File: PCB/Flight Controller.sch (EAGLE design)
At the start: 24 parts, among them J1 ZX62-AB-5PA(31), J2 M50-3600542R, U1 BMP390L, U2 NINA-B306, U3 LMS8117ADT-3.3, U4 BNO055

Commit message: added power and PWM pinheaders to schematic
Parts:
- added JP1: (no value), pinhead:PINHD-1X2
- added JP2, JP3: (no value), pinhead:PINHD-1X4
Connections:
- net GND: now also JP1.2, JP2.1, JP2.3, JP3.1, JP3.3
- net PWM0: now also JP2.2
- net PWM1: now also JP2.4
- net PWM2: now also JP3.2
- net PWM3: now also JP3.4
- net VCC: now also JP1.1
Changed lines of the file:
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@@
 <part name="GND16" library="supply1" library_urn="urn:adsk.eagle:library:371" deviceset="GND" device=""/>
 <part name="GND17" library="supply1" library_urn="urn:adsk.eagle:library:371" deviceset="GND" device=""/>
+<part name="JP1" library="pinhead" library_urn="urn:adsk.eagle:library:325" deviceset="PINHD-1X2" device="" package3d_urn="urn:adsk.eagle:package:22435/2"/>
+<part name="P+2" library="supply1" library_urn="urn:adsk.eagle:library:371" deviceset="VCC" device=""/>
+<part name="GND18" library="supply1" library_urn="urn:adsk.eagle:library:371" deviceset="GND" device=""/>
+<part name="JP2" library="pinhead" library_urn="urn:adsk.eagle:library:325" deviceset="PINHD-1X4" device="" package3d_urn="urn:adsk.eagle:package:22407/2"/>
+<part name="JP3" library="pinhead" library_urn="urn:adsk.eagle:library:325" deviceset="PINHD-1X4" device="" package3d_urn="urn:adsk.eagle:package:22407/2"/>
+<part name="GND19" library="supply1" library_urn="urn:adsk.eagle:library:371" deviceset="GND" device=""/>
+<part name="GND20" library="supply1" library_urn="urn:adsk.eagle:library:371" deviceset="GND" device=""/>
+<part name="GND21" library="supply1" library_urn="urn:adsk.eagle:library:371" deviceset="GND" device=""/>
+<part name="GND22" library="supply1" library_urn="urn:adsk.eagle:library:371" deviceset="GND" device=""/>
 </parts>
 <sheets>
@@
 <attribute name="VALUE" x="152.4" y="134.62" size="1.778" layer="96"/>
 </instance>
+<instance part="JP1" gate="G$1" x="45.72" y="137.16" smashed="yes" rot="R270">
+<attribute name="NAME" x="51.435" y="143.51" size="1.778" layer="95" rot="R270"/>
+<attribute name="VALUE" x="40.64" y="143.51" size="1.778" layer="96" rot="R270"/>
+</instance>
+<instance part="P+2" gate="VCC" x="50.8" y="152.4" smashed="yes">
+<attribute name="VALUE" x="48.26" y="149.86" size="1.778" layer="96" rot="R90"/>
+</instance>
+<instance part="GND18" gate="1" x="40.64" y="152.4" smashed="yes" rot="R180">
+<attribute name="VALUE" x="43.18" y="154.94" size="1.778" layer="96" rot="R180"/>
+</instance>
+<instance part="JP2" gate="A" x="342.9" y="139.7" smashed="yes">
+<attribute name="NAME" x="336.55" y="147.955" size="1.778" layer="95"/>
+<attribute name="VALUE" x="336.55" y="132.08" size="1.778" layer="96"/>
+</instance>
+<instance part="JP3" gate="A" x="342.9" y="121.92" smashed="yes">
+<attribute name="NAME" x="336.55" y="130.175" size="1.778" layer="95"/>
+<attribute name="VALUE" x="336.55" y="114.3" size="1.778" layer="96"/>
+</instance>
+<instance part="GND19" gate="1" x="314.96" y="139.7" smashed="yes">
+<attribute name="VALUE" x="312.42" y="137.16" size="1.778" layer="96"/>
+</instance>
+<instance part="GND20" gate="1" x="314.96" y="132.08" smashed="yes">
+<attribute name="VALUE" x="312.42" y="129.54" size="1.778" layer="96"/>
+</instance>
+<instance part="GND21" gate="1" x="314.96" y="121.92" smashed="yes">
+<attribute name="VALUE" x="312.42" y="119.38" size="1.778" layer="96"/>
+</instance>
+<instance part="GND22" gate="1" x="314.96" y="114.3" smashed="yes">
+<attribute name="VALUE" x="312.42" y="111.76" size="1.778" layer="96"/>
+</instance>
 </instances>
 <busses>
@@
 <wire x1="-10.16" y1="114.3" x2="-10.16" y2="109.22" width="0.1524" layer="91"/>
 <junction x="-10.16" y="114.3"/>
+</segment>
+<segment>
+<pinref part="JP1" gate="G$1" pin="1"/>
+<wire x1="48.26" y1="139.7" x2="48.26" y2="144.78" width="0.1524" layer="91"/>
+<wire x1="48.26" y1="144.78" x2="50.8" y2="144.78" width="0.1524" layer="91"/>
+<pinref part="P+2" gate="VCC" pin="VCC"/>
+<wire x1="50.8" y1="144.78" x2="50.8" y2="149.86" width="0.1524" layer="91"/>
 </segment>
 </net>
@@
 <pinref part="GND17" gate="1" pin="GND"/>
 </segment>
+<segment>
+<pinref part="GND18" gate="1" pin="GND"/>
+<wire x1="40.64" y1="149.86" x2="40.64" y2="144.78" width="0.1524" layer="91"/>
+<wire x1="40.64" y1="144.78" x2="45.72" y2="144.78" width="0.1524" layer="91"/>
+<pinref part="JP1" gate="G$1" pin="2"/>
+<wire x1="45.72" y1="144.78" x2="45.72" y2="139.7" width="0.1524" layer="91"/>
+</segment>
+<segment>
+<pinref part="JP2" gate="A" pin="1"/>
+<wire x1="340.36" y1="144.78" x2="314.96" y2="144.78" width="0.1524" layer="91"/>
+<pinref part="GND19" gate="1" pin="GND"/>
+<wire x1="314.96" y1="144.78" x2="314.96" y2="142.24" width="0.1524" layer="91"/>
+</segment>
+<segment>
+<pinref part="JP2" gate="A" pin="3"/>
+<wire x1="340.36" y1="139.7" x2="320.04" y2="139.7" width="0.1524" layer="91"/>
+<wire x1="320.04" y1="139.7" x2="320.04" y2="137.16" width="0.1524" layer="91"/>
+<wire x1="320.04" y1="137.16" x2="314.96" y2="137.16" width="0.1524" layer="91"/>
+<pinref part="GND20" gate="1" pin="GND"/>
+<wire x1="314.96" y1="137.16" x2="314.96" y2="134.62" width="0.1524" layer="91"/>
+</segment>
+<segment>
+<pinref part="GND21" gate="1" pin="GND"/>
+<wire x1="314.96" y1="124.46" x2="314.96" y2="127" width="0.1524" layer="91"/>
+<pinref part="JP3" gate="A" pin="1"/>
+<wire x1="314.96" y1="127" x2="340.36" y2="127" width="0.1524" layer="91"/>
+</segment>
+<segment>
+<pinref part="JP3" gate="A" pin="3"/>
+<wire x1="340.36" y1="121.92" x2="320.04" y2="121.92" width="0.1524" layer="91"/>
+<wire x1="320.04" y1="121.92" x2="320.04" y2="116.84" width="0.1524" layer="91"/>
+<pinref part="GND22" gate="1" pin="GND"/>
+<wire x1="320.04" y1="116.84" x2="314.96" y2="116.84" width="0.1524" layer="91"/>
+</segment>
 </net>
 <net name="D-" class="0">
@@
 <label x="246.38" y="55.88" size="1.778" layer="95"/>
 </segment>
+<segment>
+<pinref part="JP2" gate="A" pin="2"/>
+<wire x1="340.36" y1="142.24" x2="335.28" y2="142.24" width="0.1524" layer="91"/>
+<label x="327.66" y="142.24" size="1.778" layer="95"/>
+</segment>
 </net>
 <net name="PWM1" class="0">
@@
 <label x="246.38" y="53.34" size="1.778" layer="95"/>
 </segment>
+<segment>
+<pinref part="JP2" gate="A" pin="4"/>
+<wire x1="340.36" y1="137.16" x2="335.28" y2="137.16" width="0.1524" layer="91"/>
+<label x="327.66" y="137.16" size="1.778" layer="95"/>
+</segment>
 </net>
 <net name="PWM2" class="0">
@@
 <label x="246.38" y="50.8" size="1.778" layer="95"/>
 </segment>
+<segment>
+<pinref part="JP3" gate="A" pin="2"/>
+<wire x1="340.36" y1="124.46" x2="335.28" y2="124.46" width="0.1524" layer="91"/>
+<label x="327.66" y="124.46" size="1.778" layer="95"/>
+</segment>
 </net>
 <net name="PWM3" class="0">
@@
 <label x="246.38" y="48.26" size="1.778" layer="95"/>
 </segment>
-</net>
+<segment>
+<pinref part="JP3" gate="A" pin="4"/>
+<wire x1="340.36" y1="119.38" x2="335.28" y2="119.38" width="0.1524" layer="91"/>
+<label x="327.66" y="119.38" size="1.778" layer="95"/>
+</segment>
+</net>

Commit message: began routing PCB
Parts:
- added R8: 10k, rcl:R-US_R1206
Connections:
- net NRESET: now also R8.1
- net VDD: now also R8.2
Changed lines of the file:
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@@
 <part name="GND21" library="supply1" library_urn="urn:adsk.eagle:library:371" deviceset="GND" device=""/>
 <part name="GND22" library="supply1" library_urn="urn:adsk.eagle:library:371" deviceset="GND" device=""/>
+<part name="R8" library="rcl" library_urn="urn:adsk.eagle:library:334" deviceset="R-US_" device="R1206" package3d_urn="urn:adsk.eagle:package:23540/2" value="10k"/>
+<part name="VDD14" library="supply1" library_urn="urn:adsk.eagle:library:371" deviceset="VDD" device=""/>
 </parts>
 <sheets>
@@
 <instance part="GND22" gate="1" x="314.96" y="114.3" smashed="yes">
 <attribute name="VALUE" x="312.42" y="111.76" size="1.778" layer="96"/>
+</instance>
+<instance part="R8" gate="G$1" x="274.32" y="114.3" smashed="yes" rot="R90">
+<attribute name="NAME" x="272.8214" y="115.57" size="1.778" layer="95" rot="R90"/>
+<attribute name="VALUE" x="280.162" y="115.57" size="1.778" layer="96" rot="R90"/>
+</instance>
+<instance part="VDD14" gate="G$1" x="274.32" y="127" smashed="yes">
+<attribute name="VALUE" x="271.78" y="124.46" size="1.778" layer="96" rot="R90"/>
 </instance>
 </instances>
@@
 <wire x1="139.7" y1="162.56" x2="139.7" y2="154.94" width="0.1524" layer="91"/>
 <junction x="139.7" y="154.94"/>
+</segment>
+<segment>
+<pinref part="VDD14" gate="G$1" pin="VDD"/>
+<pinref part="R8" gate="G$1" pin="2"/>
+<wire x1="274.32" y1="124.46" x2="274.32" y2="119.38" width="0.1524" layer="91"/>
 </segment>
 </net>
@@
 <label x="246.38" y="86.36" size="1.778" layer="95"/>
 </segment>
-</net>
+<segment>
+<pinref part="R8" gate="G$1" pin="1"/>
+<wire x1="274.32" y1="109.22" x2="274.32" y2="104.14" width="0.1524" layer="91"/>
+<label x="276.86" y="104.14" size="1.778" layer="95"/>
+</segment>
+</net>

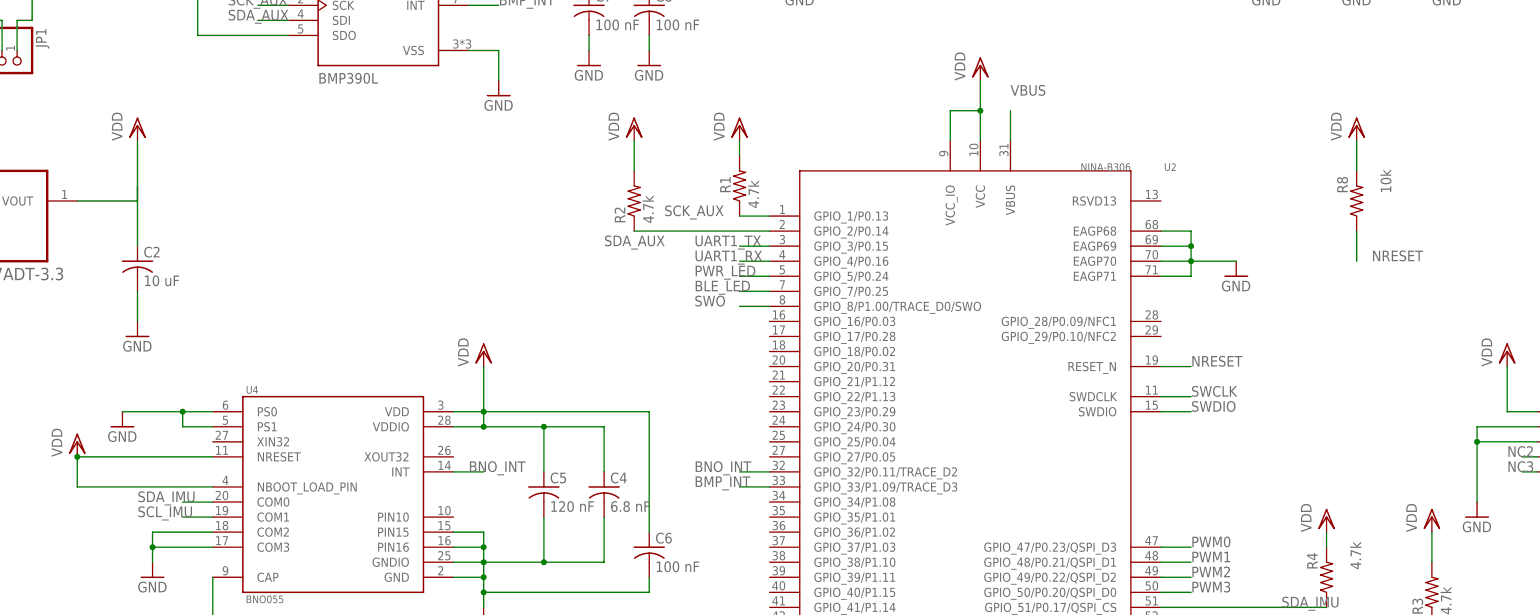
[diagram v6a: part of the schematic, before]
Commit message: continued work on PCB layout and added new headers for UARTs
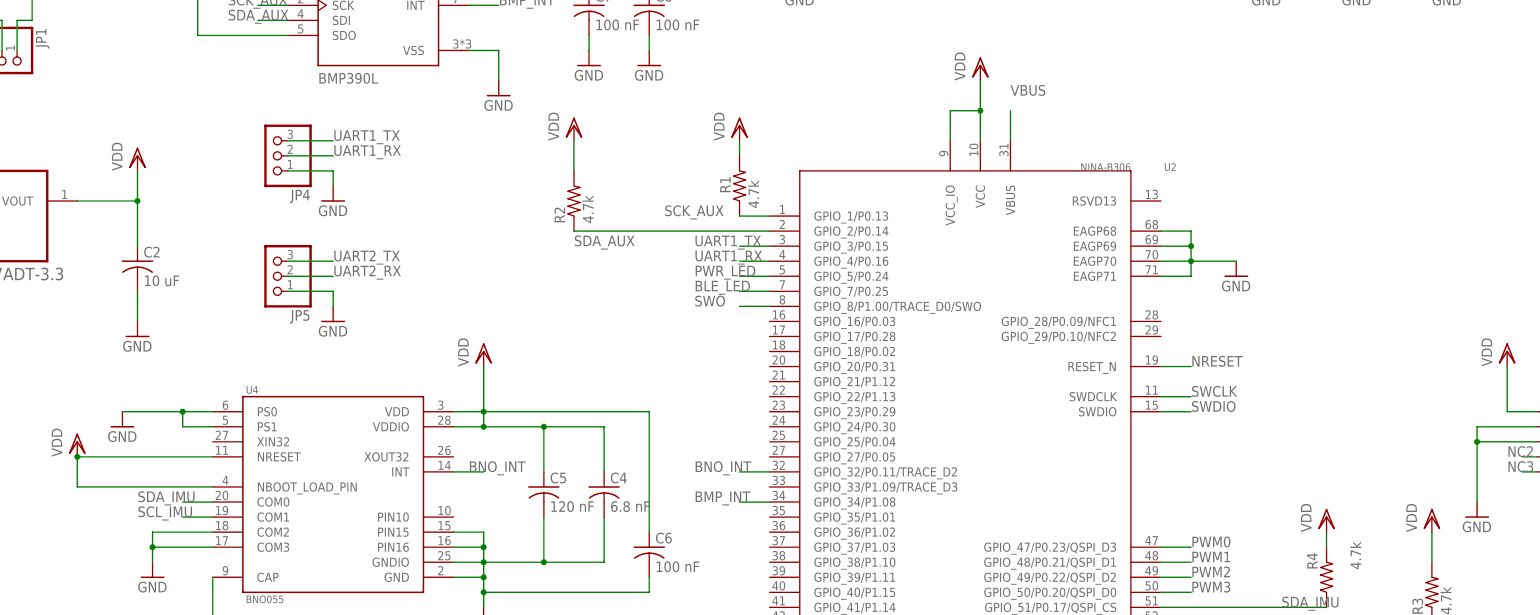
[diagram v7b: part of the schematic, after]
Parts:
- removed R8: 10k, rcl:R-US_R1206
- added JP4, JP5: (no value), pinhead:PINHD-1X3
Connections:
- removed net VCC1: C2.1
- net BMP_INT: now also U2.GPIO_34/P1.08; no longer U2.GPIO_33/P1.09/TRACE_D3
- net GND: now also JP4.1, JP5.1
- net NRESET: no longer R8.1
- net UART1_RX: now also JP4.2
- net UART1_TX: now also JP4.3
- net UART2_RX: now also JP5.2
- net UART2_TX: now also JP5.3
- net VDD: now also C2.1; no longer R8.2
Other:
- moved on the sheet: R2

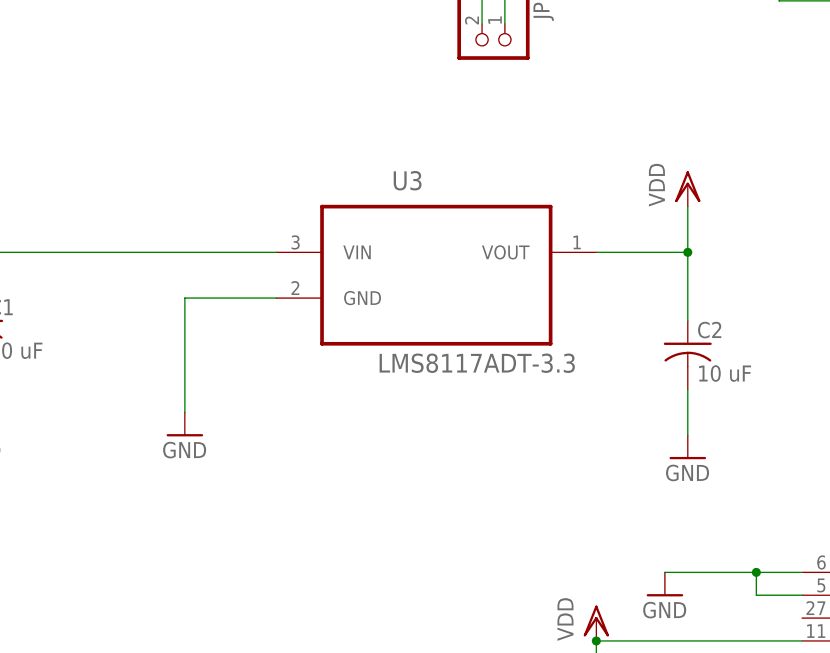
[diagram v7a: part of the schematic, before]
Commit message: replaced voltage regulator with SOT-223 package, reviewed board and is ready to order
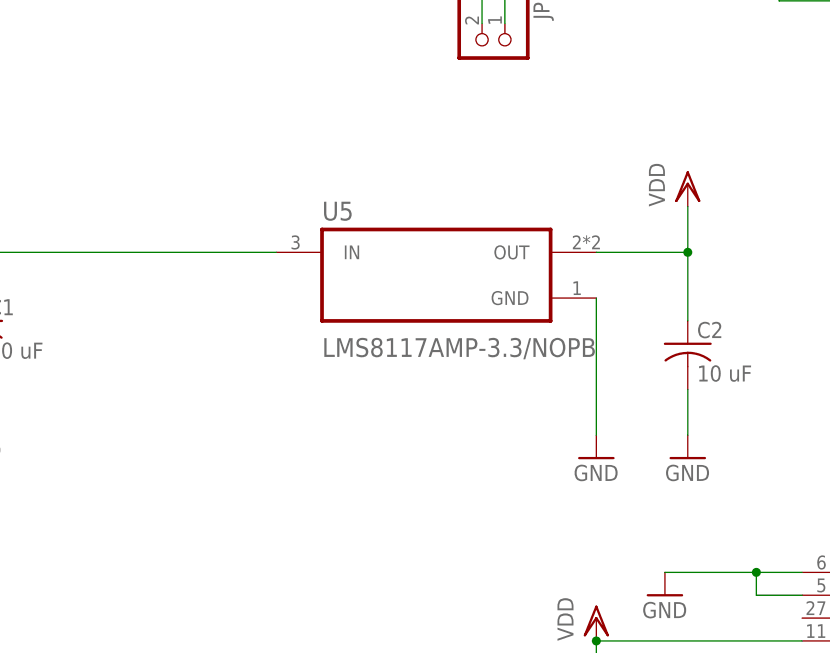
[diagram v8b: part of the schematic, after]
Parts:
- removed U3: LMS8117ADT-3.3, LMS8117ADT-3.3:LMS8117ADT-3.3
- added U5: LMS8117AMP-3.3/NOPB, LMS8117AMP-3.3_NOPB:LMS8117AMP-3.3/NOPB
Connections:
- net GND: now also U5.GND; no longer U3.GND
- net VCC: now also U5.IN; no longer U3.VIN
- net VDD: now also U5.OUT; no longer U3.VOUT
